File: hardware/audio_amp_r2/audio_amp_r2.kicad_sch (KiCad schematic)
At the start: 31 parts, among them J1 PJ-320D, J2 PJ-320D, J3 JST_PH_1x02, J6 KH-BNC50-3511, J7 KH-BNC50-3511, J8 Conn_01x04_Pin, U1 AD8397

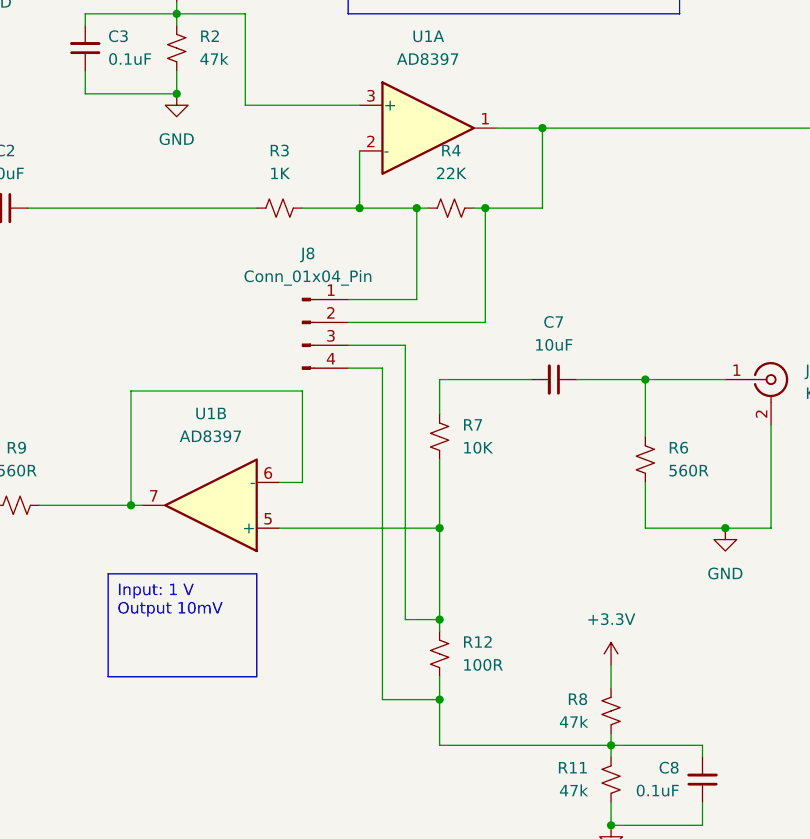
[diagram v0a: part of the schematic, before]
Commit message: update input / output gain levels
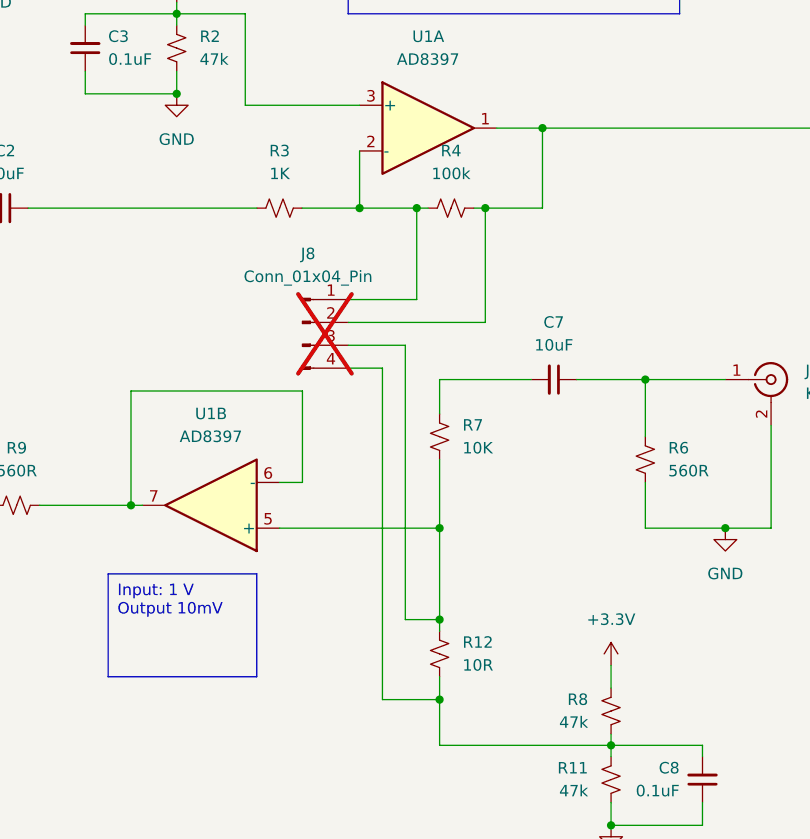
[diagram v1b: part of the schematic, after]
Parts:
- J8: now not fitted; now left out of the parts list
- R12: value 100R -> 10R; JLCPCB Part # C17408 -> C17415
- R4: value 22K -> 100k; JLCPCB Part # C17560 -> C149504
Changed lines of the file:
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@@
   )
   (symbol (lib_id "Connector:Conn_01x04_Pin") (at 149.86 82.55 0) (unit 1)
-    (in_bom yes) (on_board yes) (dnp no) (fields_autoplaced)
+    (in_bom no) (on_board yes) (dnp yes) (fields_autoplaced)
     (property "Reference" "J8" (at 150.495 74.93 0)
       (effects (font (size 1.27 1.27)))
@@
       (effects (font (size 1.27 1.27)))
     )
-    (property "Value" "22K" (at 166.37 66.04 90)
+    (property "Value" "100k" (at 166.37 66.04 90)
       (effects (font (size 1.27 1.27)))
     )
@@
       (effects (font (size 1.27 1.27)) hide)
     )
-    (property "Datasheet" "~" (at 166.37 69.85 0)
-      (effects (font (size 1.27 1.27)) hide)
-    )
-    (property "JLCPCB Part #" "C17560" (at 166.37 69.85 0)
+    (property "Datasheet" "" (at 166.37 69.85 0)
+      (effects (font (size 1.27 1.27)) hide)
+    )
+    (property "JLCPCB Part #" "C149504" (at 166.37 69.85 0)
       (effects (font (size 1.27 1.27)) hide)
     )
@@
       (effects (font (size 1.27 1.27)) (justify left))
     )
-    (property "Value" "100R" (at 167.64 120.65 0)
+    (property "Value" "10R" (at 167.64 120.65 0)
       (effects (font (size 1.27 1.27)) (justify left))
     )
@@
       (effects (font (size 1.27 1.27)) hide)
     )
-    (property "Datasheet" "~" (at 165.1 119.38 0)
-      (effects (font (size 1.27 1.27)) hide)
-    )
-    (property "JLCPCB Part #" "C17408" (at 165.1 119.38 0)
-      (effects (font (size 1.27 1.27)) hide)
-    )
+    (property "Datasheet" "" (at 165.1 119.38 0)
+      (effects (font (size 1.27 1.27)) hide)
+    )
+    (property "JLCPCB Part #" "C17415" (at 165.1 119.38 0)
+      (effects (font (size 1.27 1.27)) hide)
+    )

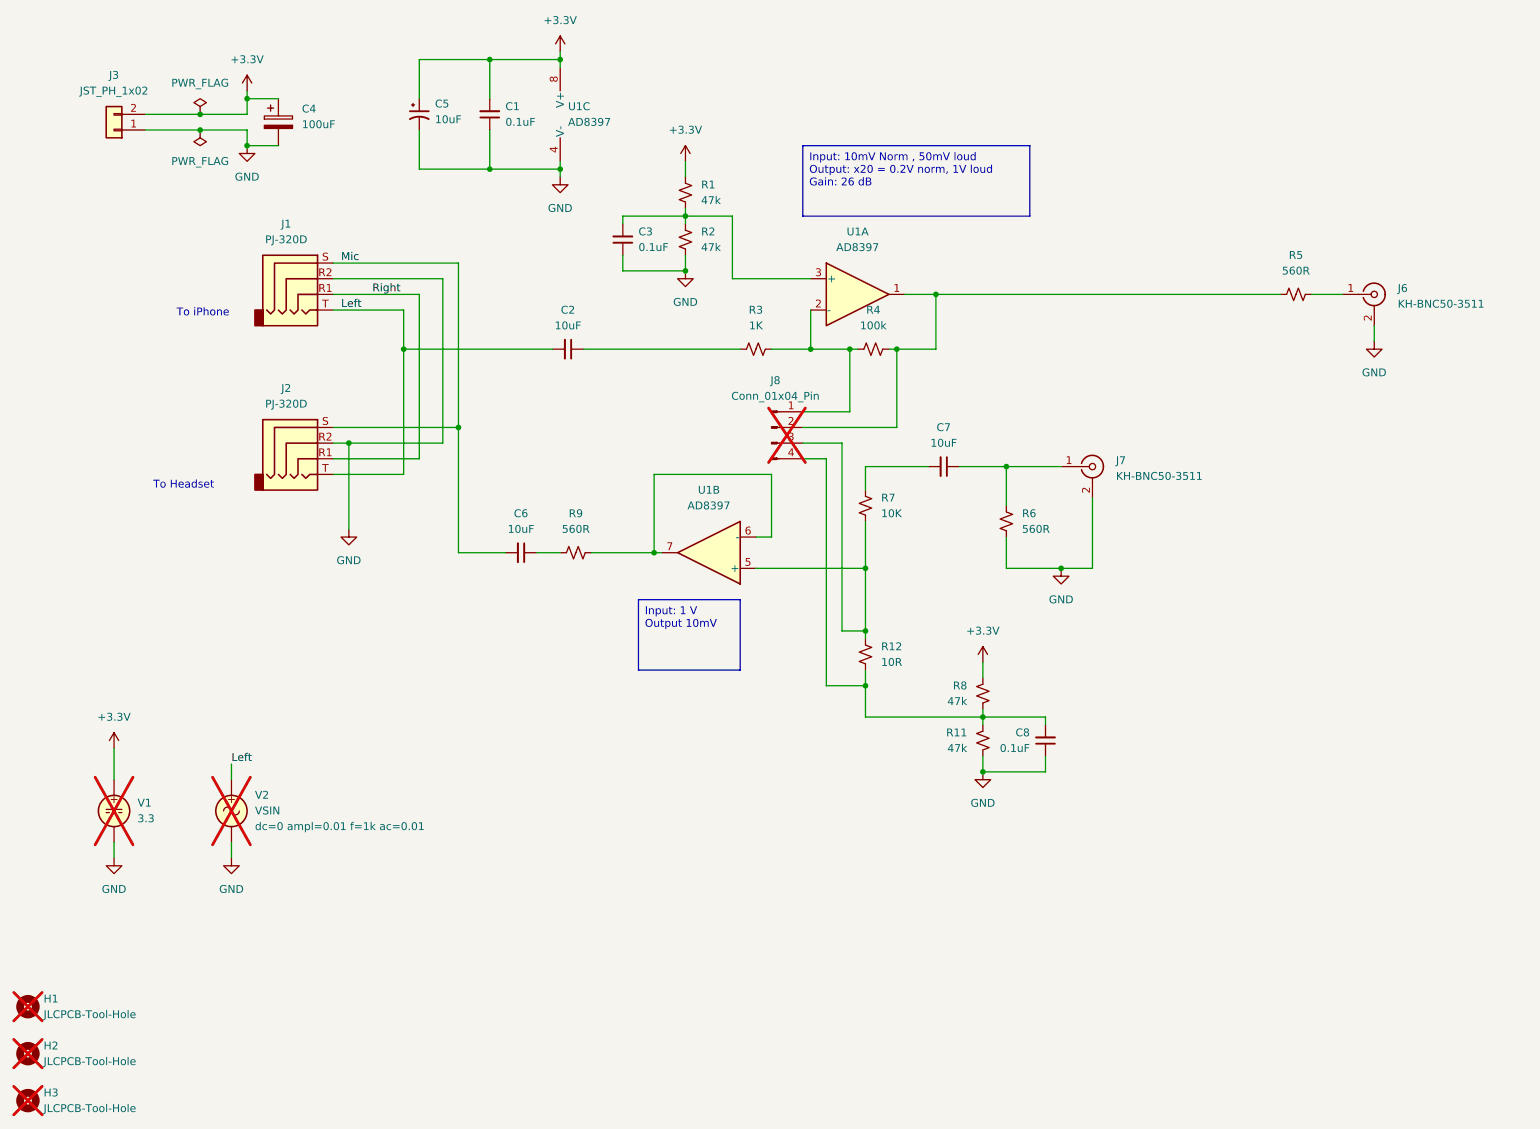
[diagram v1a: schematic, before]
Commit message: add power supply to audio test board
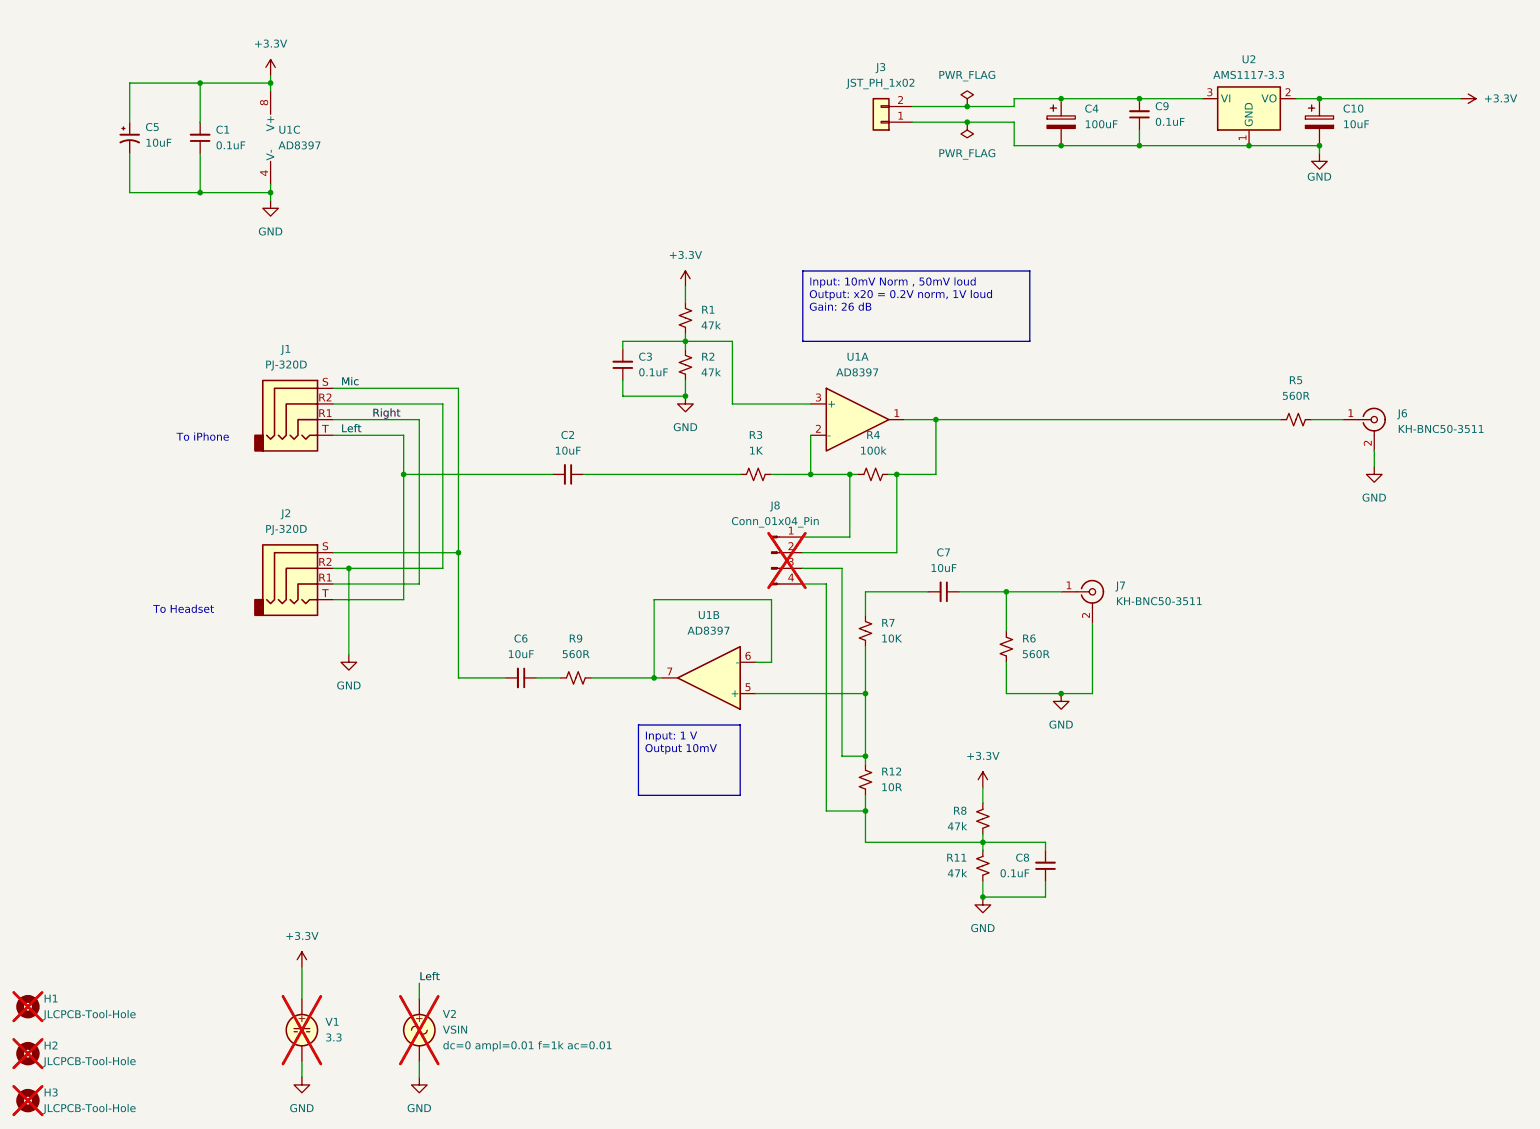
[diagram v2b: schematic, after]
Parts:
- added C10: 10uF, Capacitor_Tantalum_SMD:CP_EIA-3216-18_Kemet-A, symbol Device:C_Polarized
- added C9: 0.1uF, Capacitor_SMD:C_0805_2012Metric, symbol Device:C_Small
- added U2: AMS1117-3.3, Package_TO_SOT_SMD:SOT-223-3_TabPin2, symbol Regulator_Linear:AMS1117-3.3
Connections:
- net +3.3V: now also C10.1, U2.2 (VO); no longer C4.1, J3.2 (Pin_2)
- net GND: now also C10.2, C9.1, U2.1 (GND)
- new net: C4.1, C9.2, J3.2 (Pin_2), U2.3 (VI)
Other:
- moved on the sheet: C1, C2, C3, C4, C5, C6, C7, C8, J1, J2, J3, J6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

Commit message: move audio board to R2 build
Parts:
- C10: JLCPCB Part # (none) -> C7171; LCSC C7171 -> (none)
- U2: JLCPCB Part # (none) -> C6186; LCSC C6186 -> (none)
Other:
- moved on the sheet: C2, C6, C7, C8, J1, J2, J7, R11, R6, R8, R9

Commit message: version sent for R2build of audio amp HW
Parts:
- J8: now in the parts list
- U1: JLCPCB Part # C578714 -> C90876
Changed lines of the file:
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@@
   )
   (symbol (lib_id "Connector:Conn_01x04_Pin") (at 149.86 102.87 0) (unit 1)
-    (in_bom no) (on_board yes) (dnp yes) (fields_autoplaced)
+    (in_bom yes) (on_board yes) (dnp yes) (fields_autoplaced)
     (property "Reference" "J8" (at 150.495 95.25 0)
       (effects (font (size 1.27 1.27)))
@@
       (effects (font (size 1.27 1.27)) hide)
     )
-    (property "JLCPCB Part #" "C578714" (at 139.7 123.19 0)
+    (property "JLCPCB Part #" "C90876" (at 139.7 123.19 0)
       (effects (font (size 1.27 1.27)) hide)
     )
@@
       (effects (font (size 1.27 1.27)) hide)
     )
-    (property "JLCPCB Part #" "C578714" (at 71.12 35.56 0)
+    (property "JLCPCB Part #" "C90876" (at 71.12 35.56 0)
       (effects (font (size 1.27 1.27)) hide)
     )
@@
       (effects (font (size 1.27 1.27)) hide)
     )
-    (property "JLCPCB Part #" "C578714" (at 163.83 81.28 0)
-      (effects (font (size 1.27 1.27)) hide)
-    )
+    (property "JLCPCB Part #" "C90876" (at 163.83 81.28 0)
+      (effects (font (size 1.27 1.27)) hide)
+    )
